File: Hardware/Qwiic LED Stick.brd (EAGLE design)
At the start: 91.4 x 25.4 mm, 66 parts, among them J2 QWIIC_RA, J4 QWIIC_RA, J6 AVR_SPI_PROG_3X2TESTPOINTS, U2 ATTINY85

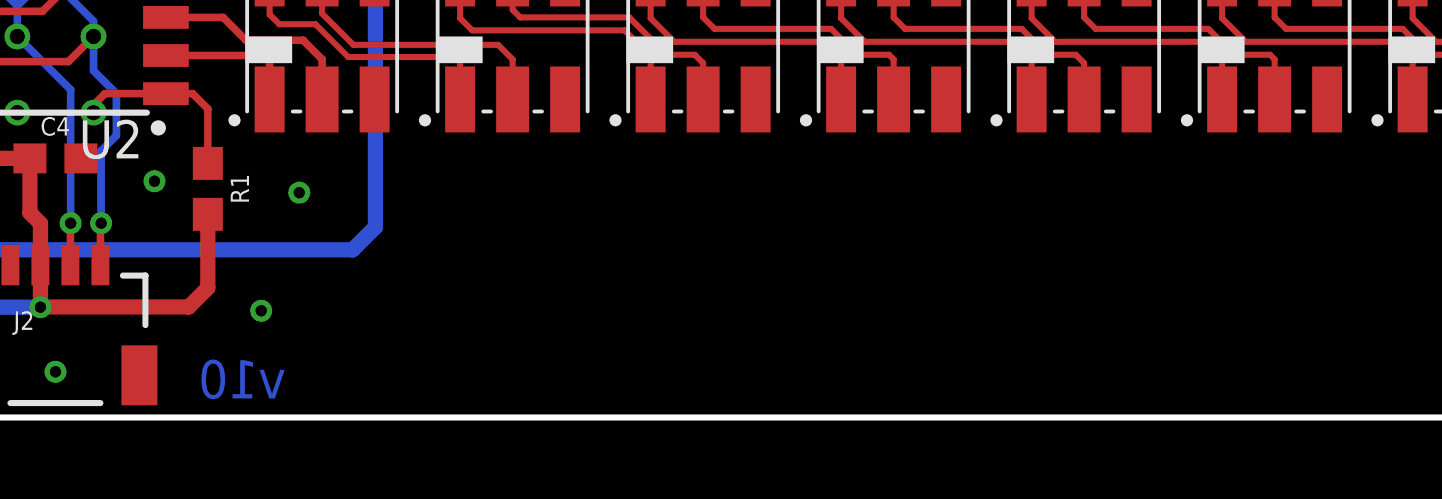
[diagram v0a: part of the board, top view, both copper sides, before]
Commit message: Update logos
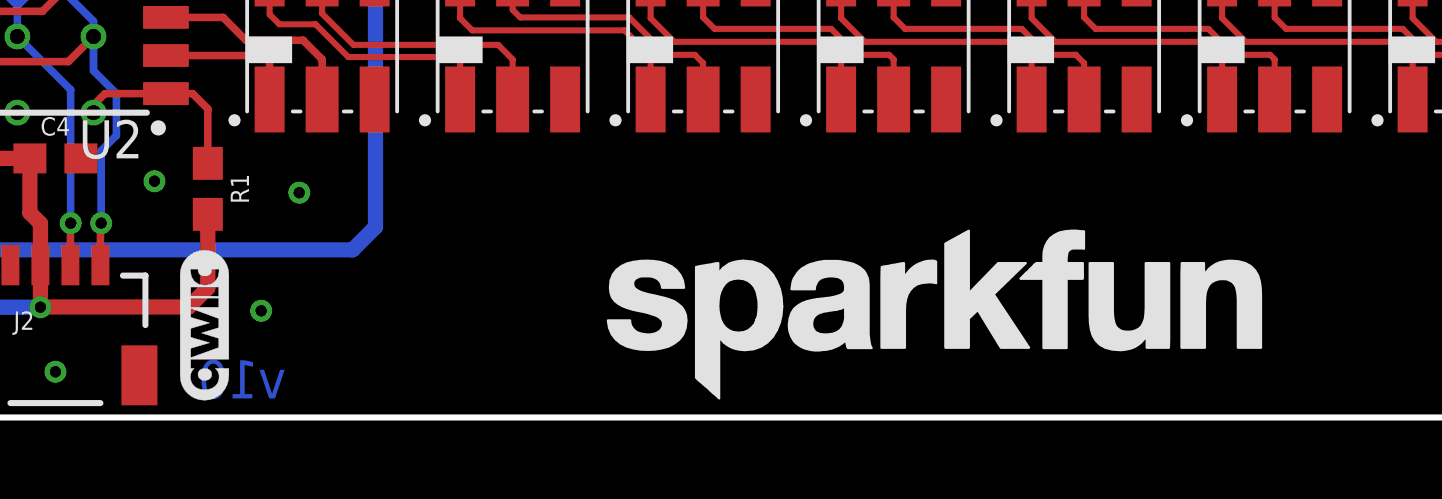
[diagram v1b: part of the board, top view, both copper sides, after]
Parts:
- added LOGO2, LOGO5: SFE_LOGO_NAME.2_INCH, SparkFun-Aesthetics:SFE_LOGO_NAME_.2
- added LOGO3: QWIIC_LOGO_5MM, SparkFun-Aesthetics:QWIIC_5MM
- added LOGO4: SFE_LOGO_FLAME.2_INCH, SparkFun-Aesthetics:SFE_LOGO_FLAME_.2
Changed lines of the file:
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@@
 <drawing>
 <settings>
-<setting alwaysvectorfont="no"/>
+<setting alwaysvectorfont="yes"/>
 <setting keepoldvectorfont="yes"/>
 <setting verticaltext="up"/>
@@
 <attribute name="VALUE" x="3.302" y="10.16" size="0.6096" layer="27" font="vector" ratio="20" rot="R90"/>
 </element>
+<element name="LOGO2" library="SparkFun-Aesthetics" package="SFE_LOGO_NAME_.2" value="SFE_LOGO_NAME.2_INCH" x="45.847" y="3.429" smashed="yes"/>
+<element name="LOGO3" library="SparkFun-Aesthetics" package="QWIIC_5MM" value="QWIIC_LOGO_5MM" x="21.463" y="3.048" smashed="yes" rot="R90"/>
+<element name="LOGO4" library="SparkFun-Aesthetics" package="SFE_LOGO_FLAME_.2" value="SFE_LOGO_FLAME.2_INCH" x="43.561" y="15.367" smashed="yes" rot="MR0"/>
+<element name="LOGO5" library="SparkFun-Aesthetics" package="SFE_LOGO_NAME_.2" value="SFE_LOGO_NAME.2_INCH" x="46.99" y="10.16" smashed="yes" rot="MR0"/>
 </elements>
 <signals>

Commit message: New buzzard labels
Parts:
- removed U$28: (no value), buzzard_labels (5):ADDR2
- removed U$30: (no value), buzzard_power:3#3V3
- removed U$31: (no value), buzzard_power:VCC1
- removed U$32: (no value), buzzard_labels (6):QWIIC_LED_STICK1
- added U$1, U$2: (no value), output:#GND#0
- added U$14: (no value), output:#3#3V#0
- U$10: device Labels-0_04:(PWR) -> output:#ADDR#0
- U$12: device Labels-0_04:GND1 -> output:#VLED#0
- U$13: device buzzard_labels (6):QWIIC_LED_STICK1 -> output:QWIIC_LED_STICK0
- U$15: device buzzard_labels (5):DO12 -> output:#_DO#0
- U$16: device buzzard_labels (5):CO9 -> output:#_CO#0
- U$17: device buzzard_labels (5):SDA0 -> output:#3#3V#0
- U$18: device buzzard_labels (5):SCL1 -> output:#VCC#0
- U$19: device buzzard_power:VCC1 -> output:#VCC#0
- U$20: device buzzard_power:VCC1 -> output:#SDA#0
- U$21: device Labels-0_04:3#3V2 -> output:#SDA_#0
- U$22: device Labels-0_04:GND1 -> output:#SCL#0
- U$23: device buzzard_power:GND0 -> output:#SCL_#0
- U$24: device buzzard_power:GND0 -> output:#LED#0
- U$25: device buzzard_labels (5):VLED3 -> output:#VCC#0
- U$26: device Labels-0_04:SCL9 -> output:PWR0
- U$27: device Labels-0_04:SDA8 -> output:QWIIC_LED_STICK0
- U$3, U$8: device Labels-0_04:GND1 -> output:#GND#0
- U$4: device Labels-0_04:3#3V2 -> output:#GND#0
- U$5: device buzzard_labels (5):VLED4 -> output:#GND#0
- U$6: device buzzard_labels (5):DO8 -> output:#CO#0
- U$7: device buzzard_labels (5):CO5 -> output:#DO#0
- U$9: device buzzard_labels (5):VLED4 -> output:#VLED#0
- moved U$27 54.9 mm to (55.9, 21.6), flipped to the bottom
- moved U$10 26.6 mm to (29.2, 16.5), flipped to the bottom
- moved U$13 16.8 mm to (36.8, 21.6), flipped to the top
- moved U$25 13.6 mm to (16.8, 8.51)
- moved U$24 12.4 mm to (12.7, 1.02), flipped to the bottom
- moved U$12 9.02 mm to (89.9, 16.5), flipped to the bottom
- moved U$5 8.95 mm to (85.3, 8.89), flipped to the top
- moved U$26 8.41 mm to (5.08, 3.81)
- moved U$22 7.62 mm to (1.65, 11.4)
- moved U$20 6.83 mm to (1.65, 14.0), flipped to the top
- moved U$11 6.14 mm to (10.8, 21.0)
- moved U$21 5.23 mm to (6.10, 14.0), flipped to the bottom
- moved U$23 5.11 mm to (5.84, 11.4)
- moved U$18 5.01 mm to (1.65, 8.89), flipped to the top
- moved U$19 4.70 mm to (6.22, 8.89), flipped to the bottom
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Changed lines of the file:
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@@
 <?xml version="1.0" encoding="utf-8"?>
 <!DOCTYPE eagle SYSTEM "eagle.dtd">
-<eagle version="9.5.2">
+<eagle version="9.6.2">
 <drawing>
 <settings>
@@
 <element name="JP1" library="SparkFun-Aesthetics" package="FIDUCIAL-MICRO" value="FIDUCIALUFIDUCIAL" x="0.762" y="0.762" smashed="yes" rot="MR270"/>
 <element name="JP5" library="SparkFun-Aesthetics" package="FIDUCIAL-MICRO" value="FIDUCIALUFIDUCIAL" x="90.551" y="24.511" smashed="yes" rot="MR270"/>
-<element name="U$21" library="Labels-0_04" package="3#3V2" value="" x="1.524" y="16.51" smashed="yes"/>
-<element name="U$22" library="Labels-0_04" package="GND1" value="" x="1.524" y="19.05" smashed="yes"/>
-<element name="U$26" library="Labels-0_04" package="SCL9" value="" x="1.524" y="11.43" smashed="yes"/>
-<element name="U$27" library="Labels-0_04" package="SDA8" value="" x="1.524" y="13.97" smashed="yes"/>
-<element name="U$3" library="Labels-0_04" package="GND1" value="" x="6.35" y="19.05" smashed="yes" rot="MR0"/>
-<element name="U$4" library="Labels-0_04" package="3#3V2" value="" x="6.477" y="16.51" smashed="yes" rot="MR0"/>
 <element name="R3" library="SparkFun-Resistors" package="0603" value="1k" x="7.62" y="1.016" smashed="yes" rot="R180">
 <attribute name="NAME" x="7.62" y="0.254" size="0.6096" layer="25" font="vector" ratio="20" rot="R180" align="bottom-center"/>
@@
 <attribute name="VALUE" x="7.62" y="3.175" size="0.6096" layer="27" font="vector" ratio="20" rot="R180" align="top-center"/>
 </element>
-<element name="U$10" library="Labels-0_04" package="(PWR)" value="" x="5.715" y="3.937" smashed="yes"/>
-<element name="U$11" library="Labels-0_04" package="(I_SUPER2_C)" value="" x="10.033" y="14.859" smashed="yes" rot="MR0"/>
+<element name="U$11" library="Labels-0_04" package="(I_SUPER2_C)" value="" x="10.795" y="20.955" smashed="yes" rot="MR0"/>
 <element name="D3" library="SparkFun-LED" package="APA102-5050" value="APA102-5050" x="25.4" y="12.7" smashed="yes">
 <attribute name="NAME" x="25.44" y="16.455" size="0.6096" layer="25" font="vector" ratio="20" align="bottom-center"/>
@@
 <attribute name="VALUE" x="92.202" y="17.78" size="0.6096" layer="28" font="vector" ratio="20" rot="MR270"/>
 </element>
-<element name="U$9" library="buzzard_labels (5)" package="VLED4" value="" x="84.328" y="16.51" smashed="yes"/>
-<element name="U$12" library="Labels-0_04" package="GND1" value="" x="85.09" y="8.89" smashed="yes"/>
-<element name="U$15" library="buzzard_labels (5)" package="DO12" value="" x="85.979" y="11.43" smashed="yes"/>
-<element name="U$16" library="buzzard_labels (5)" package="CO9" value="" x="85.979" y="13.97" smashed="yes"/>
-<element name="U$17" library="buzzard_labels (5)" package="SDA0" value="" x="6.223" y="13.97" smashed="yes" rot="MR0"/>
-<element name="U$18" library="buzzard_labels (5)" package="SCL1" value="" x="5.969" y="11.43" smashed="yes" rot="MR0"/>
-<element name="U$5" library="buzzard_labels (5)" package="VLED4" value="" x="90.043" y="16.51" smashed="yes" rot="MR0"/>
-<element name="U$6" library="buzzard_labels (5)" package="DO8" value="" x="89.916" y="11.43" smashed="yes" rot="MR0"/>
-<element name="U$7" library="buzzard_labels (5)" package="CO5" value="" x="89.916" y="13.97" smashed="yes" rot="MR0"/>
-<element name="U$8" library="Labels-0_04" package="GND1" value="" x="89.916" y="8.89" smashed="yes" rot="MR0"/>
-<element name="U$19" library="buzzard_power" package="VCC1" value="" x="1.524" y="8.89" smashed="yes"/>
-<element name="U$20" library="buzzard_power" package="VCC1" value="" x="6.223" y="8.89" smashed="yes" rot="MR0"/>
-<element name="U$23" library="buzzard_power" package="GND0" value="" x="6.35" y="6.35" smashed="yes" rot="MR0"/>
-<element name="U$24" library="buzzard_power" package="GND0" value="" x="1.524" y="6.35" smashed="yes"/>
-<element name="U$25" library="buzzard_labels (5)" package="VLED3" value="" x="29.718" y="12.7" smashed="yes" rot="MR0"/>
-<element name="U$28" library="buzzard_labels (5)" package="ADDR2" value="" x="15.621" y="10.414" smashed="yes" rot="MR0"/>
-<element name="U$30" library="buzzard_power" package="3#3V3" value="" x="25.4" y="15.367" smashed="yes" rot="MR0"/>
-<element name="U$31" library="buzzard_power" package="VCC1" value="" x="25.273" y="10.033" smashed="yes" rot="MR0"/>
 <element name="C1" library="SparkFun-Capacitors" package="0603" value="4.7uF" x="7.62" y="8.001" smashed="yes" rot="R270">
 <attribute name="NAME" x="8.382" y="8.001" size="0.6096" layer="25" font="vector" ratio="20" rot="R270" align="bottom-center"/>
@@
 <attribute name="VALUE" x="6.858" y="8.001" size="0.6096" layer="27" font="vector" ratio="20" rot="R270" align="top-center"/>
 </element>
-<element name="U$32" library="buzzard_labels (6)" package="QWIIC_LED_STICK1" value="" x="37.973" y="21.082" smashed="yes"/>
-<element name="U$13" library="buzzard_labels (6)" package="QWIIC_LED_STICK1" value="" x="53.594" y="21.082" smashed="yes" rot="MR0"/>
 <element name="LED" library="SparkFun-Jumpers" package="SMT-JUMPER_2_NC_TRACE_SILK" package3d_urn="urn:adsk.eagle:package:39281/1" value="JUMPER-SMT_2_NC_TRACE_SILK" x="7.62" y="1.016" smashed="yes" rot="MR180">
 <attribute name="NAME" x="7.62" y="-0.127" size="0.6096" layer="26" font="vector" ratio="20" rot="MR180" align="bottom-center"/>
@@
 <element name="LOGO4" library="SparkFun-Aesthetics" package="SFE_LOGO_FLAME_.2" value="SFE_LOGO_FLAME.2_INCH" x="43.561" y="15.367" smashed="yes" rot="MR0"/>
 <element name="LOGO5" library="SparkFun-Aesthetics" package="SFE_LOGO_NAME_.2" value="SFE_LOGO_NAME.2_INCH" x="46.99" y="10.16" smashed="yes" rot="MR0"/>
+<element name="U$1" library="output" package="#GND#0" value="" x="1.651" y="6.35" smashed="yes"/>
+<element name="U$2" library="output" package="#GND#0" value="" x="6.096" y="6.35" smashed="yes" rot="MR0"/>
+<element name="U$3" library="output" package="#GND#0" value="" x="1.651" y="19.05" smashed="yes"/>
+<element name="U$4" library="output" package="#GND#0" value="" x="6.096" y="19.05" smashed="yes" rot="MR0"/>
+<element name="U$14" library="output" package="#3#3V#0" value="" x="1.651" y="16.51" smashed="yes"/>
+<element name="U$17" library="output" package="#3#3V#0" value="" x="6.477" y="16.51" smashed="yes" rot="MR0"/>
+<element name="U$18" library="output" package="#VCC#0" value="" x="1.651" y="8.89" smashed="yes"/>
+<element name="U$19" library="output" package="#VCC#0" value="" x="6.223" y="8.89" smashed="yes" rot="MR0"/>
+<element name="U$20" library="output" package="#SDA#0" value="" x="1.651" y="13.97" smashed="yes"/>
+<element name="U$21" library="output" package="#SDA_#0" value="" x="6.096" y="13.97" smashed="yes" rot="MR0"/>
+<element name="U$22" library="output" package="#SCL#0" value="" x="1.651" y="11.43" smashed="yes"/>
+<element name="U$23" library="output" package="#SCL_#0" value="" x="5.842" y="11.43" smashed="yes" rot="MR0"/>
+<element name="U$24" library="output" package="#LED#0" value="" x="12.7" y="1.016" smashed="yes" rot="MR0"/>
+<element name="U$26" library="output" package="PWR0" value="" x="5.08" y="3.81" smashed="yes"/>
+<element name="U$10" library="output" package="#ADDR#0" value="" x="29.21" y="16.51" smashed="yes" rot="MR0"/>
+<element name="U$25" library="output" package="#VCC#0" value="" x="16.764" y="8.509" smashed="yes" rot="MR0"/>
+<element name="U$5" library="output" package="#GND#0" value="" x="85.344" y="8.89" smashed="yes"/>
+<element name="U$8" library="output" package="#GND#0" value="" x="89.789" y="8.89" smashed="yes" rot="MR0"/>
+<element name="U$9" library="output" package="#VLED#0" value="" x="84.455" y="16.51" smashed="yes"/>
+<element name="U$12" library="output" package="#VLED#0" value="" x="89.916" y="16.51" smashed="yes" rot="MR0"/>
+<element name="U$6" library="output" package="#CO#0" value="" x="86.36" y="13.97" smashed="yes"/>
+<element name="U$7" library="output" package="#DO#0" value="" x="86.36" y="11.43" smashed="yes"/>
+<element name="U$15" library="output" package="#_DO#0" value="" x="90.297" y="11.43" smashed="yes" rot="MR0"/>
+<element name="U$16" library="output" package="#_CO#0" value="" x="90.17" y="13.97" smashed="yes" rot="MR0"/>
+<element name="U$13" library="output" package="QWIIC_LED_STICK0" value="" x="36.83" y="21.59" smashed="yes"/>
+<element name="U$27" library="output" package="QWIIC_LED_STICK0" value="" x="55.88" y="21.59" smashed="yes" rot="MR0"/>
 </elements>
 <signals>

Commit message: Update Qwiic LED Stick.brd
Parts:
- moved U$27 1.40 mm to (54.5, 21.6)
- moved U$13 1.27 mm to (35.6, 21.6)
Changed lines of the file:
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@@
 <?xml version="1.0" encoding="utf-8"?>
 <!DOCTYPE eagle SYSTEM "eagle.dtd">
-<eagle version="9.6.2">
+<eagle version="9.5.2">
 <drawing>
 <settings>
@@
 <element name="U$15" library="output" package="#_DO#0" value="" x="90.297" y="11.43" smashed="yes" rot="MR0"/>
 <element name="U$16" library="output" package="#_CO#0" value="" x="90.17" y="13.97" smashed="yes" rot="MR0"/>
-<element name="U$13" library="output" package="QWIIC_LED_STICK0" value="" x="36.83" y="21.59" smashed="yes"/>
-<element name="U$27" library="output" package="QWIIC_LED_STICK0" value="" x="55.88" y="21.59" smashed="yes" rot="MR0"/>
+<element name="U$13" library="output" package="QWIIC_LED_STICK0" value="" x="35.56" y="21.59" smashed="yes"/>
+<element name="U$27" library="output" package="QWIIC_LED_STICK0" value="" x="54.483" y="21.59" smashed="yes" rot="MR0"/>
 </elements>
 <signals>

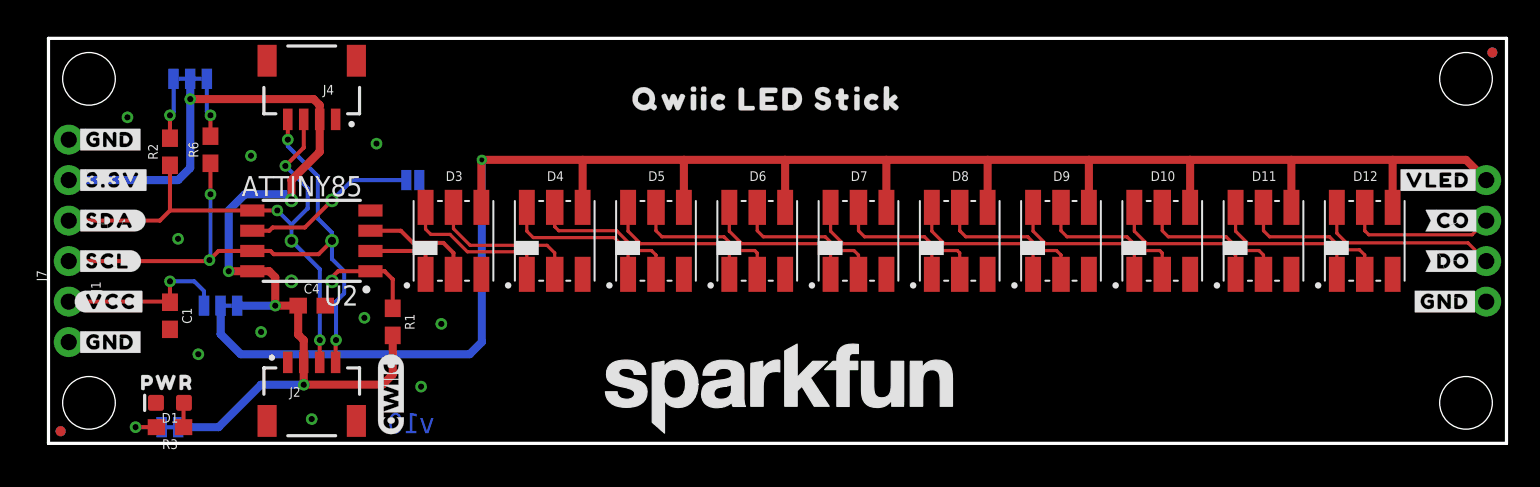
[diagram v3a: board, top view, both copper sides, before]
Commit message: Design review changes:
Sch:
Re-number diodes starting at 0
Change VCC net label to VIN
Added 4 more stand off holes for 1x1 qwiic

Board:
Added measures for PTH and LEDs
Thickened up the VIN trace to 0.02
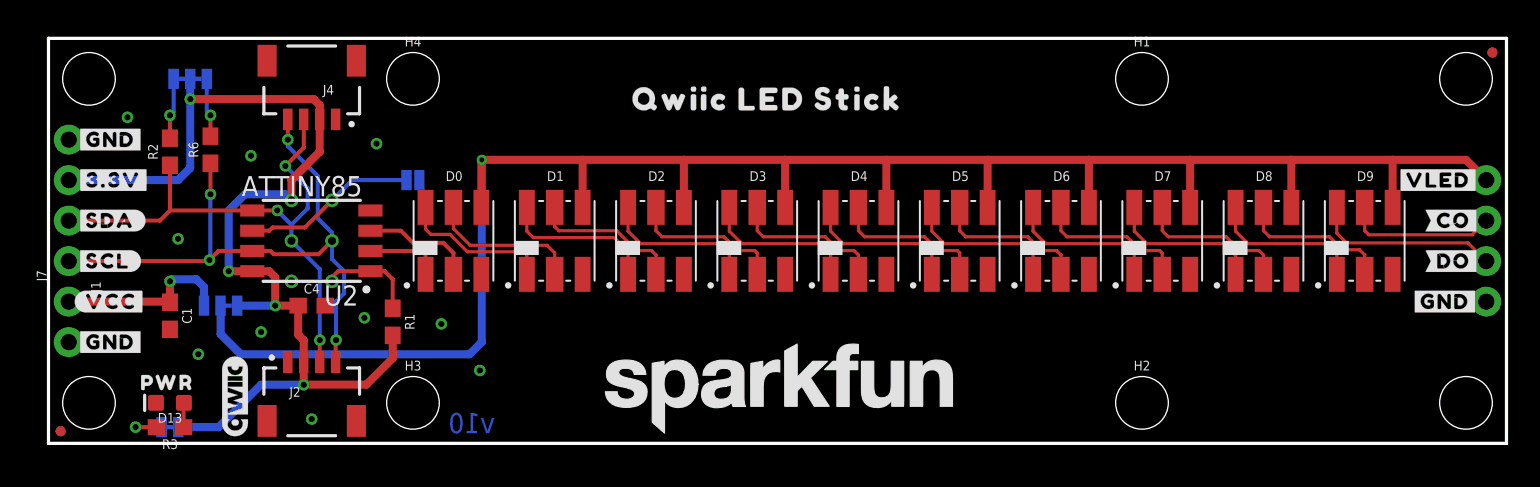
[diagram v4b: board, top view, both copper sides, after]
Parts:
- removed D10, D11, D12: APA102-5050, SparkFun-LED:APA102-5050
- added D0, D2: APA102-5050, SparkFun-LED:APA102-5050
- added D13: RED, SparkFun-LED:LED-0603
- added H1, H2, H3, H4: STAND-OFF, SparkFun-Hardware:STAND-OFF
- D1: value RED -> APA102-5050; device SparkFun-LED:LED-0603 -> SparkFun-LED:APA102-5050
- moved D1 26.2 mm to (31.8, 12.7), turned to 0 degrees
- moved D3 19.1 mm to (44.5, 12.7)
- moved D8 19.1 mm to (76.2, 12.7)
- moved D4 19.0 mm to (50.8, 12.7)
- moved D5 19.0 mm to (57.1, 12.7)
- moved D6 19.0 mm to (63.5, 12.7)
- moved D7 19.0 mm to (69.8, 12.7)
- moved D9 19.0 mm to (82.5, 12.7)
- moved LOGO3 9.78 mm to (11.7, 2.92)
- renumbered JP10 to LED_PWR
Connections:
- net VCC renamed VIN
- removed net N$10 (its old number): D10.P5, D11.P2
- removed net N$11 (its old number): D10.P6, D11.P1
- removed net N$12 (its old number): D10.P2, D9.P5
- removed net N$13 (its old number): D10.P1, D9.P6
- removed net N$8 (its old number): D11.P6, D12.P1
- removed net N$9 (its old number): D11.P5, D12.P2
- new net N$20: D2.P6, D3.P1
- new net N$21: D2.P5, D3.P2
- new net N$22: D1.P6, D2.P1
- new net N$23: D1.P5, D2.P2
- new net N$24: D0.P5, D1.P2
- new net N$25: D0.P6, D1.P1
- net CLK: now also D0.P2; no longer D3.P2
- net CO(10): now also D9.P5; no longer D12.P5
- net DO: now also D0.P1; no longer D3.P1
- net DO(10): now also D9.P6; no longer D12.P6
- net GND: now also D0.P3, D1.P3, D13.C, D2.P3; no longer D1.C, D10.P3, D11.P3, D12.P3
- net N$3: now also D13.A; no longer D1.A
- net VLED: now also D0.P4, D1.P4, D2.P4; no longer D10.P4, D11.P4, D12.P4
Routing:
- net N$22: track 0.00 -> 9.81 mm
- net N$20: track 0.00 -> 9.81 mm
- net N$8 (its old number): track 9.75 -> 0.00 mm
- net N$21: track 0.00 -> 9.73 mm
- net N$12 (its old number): track 9.73 -> 0.00 mm
- net N$13 (its old number): track 9.73 -> 0.00 mm
- net N$10 (its old number): track 9.66 -> 0.00 mm
- net N$11 (its old number): track 9.66 -> 0.00 mm
- net N$24: track 0.00 -> 9.66 mm
- net N$9 (its old number): track 9.66 -> 0.00 mm
- net N$25: track 0.00 -> 9.63 mm
- net N$23: track 0.00 -> 9.51 mm
- net 3.3V: track 67.9 -> 67.3 mm
